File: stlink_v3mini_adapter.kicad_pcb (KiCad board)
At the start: 4 copper layers, 46.5 x 18.5 mm, 19 parts, among them J1 Conn_02x07_Odd_Even, SW1 RST, U3 TLV71333PDBV

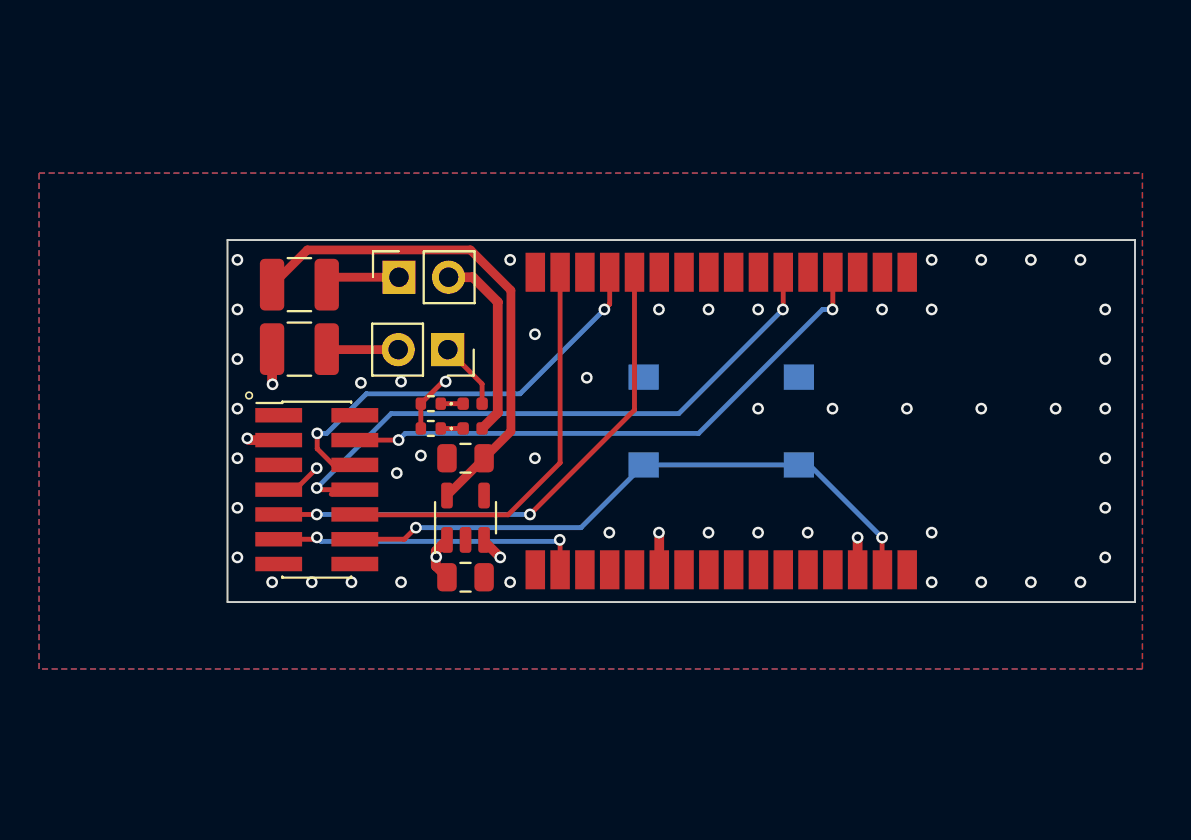
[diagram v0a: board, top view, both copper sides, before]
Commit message: add screws, switch to 2 layers
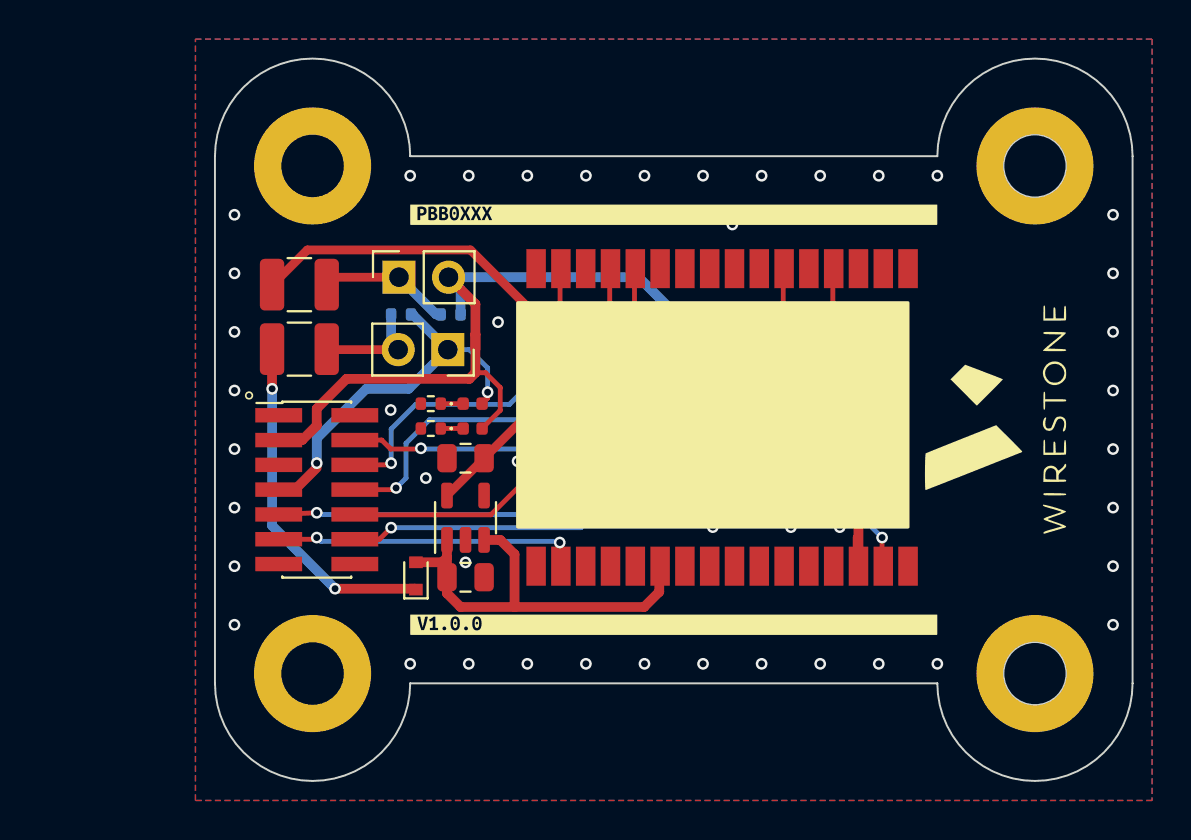
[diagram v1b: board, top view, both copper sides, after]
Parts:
- removed kibuzzard-63CA6A29: G***, kibuzzard-63CA6A29
- removed kibuzzard-63CA6A34: G***, kibuzzard-63CA6A34
- added D3: D_Schottky, Diode_SMD:D_SOD-523, F.Cu at (66.3, 83.5)
- added G***: LOGO, stlink_v3mini:wirestone, F.Cu at (96.0, 75.5)
- added G***: LOGO, stlink_v3mini:wirestone, B.Cu at (95.5, 75.5)
- added R3: R, Resistor_SMD:R_0402_1005Metric, B.Cu at (68.1, 70.1)
- added R4: R, Resistor_SMD:R_0402_1005Metric, B.Cu at (65.5, 70.1)
- added REF**: MountingHole_3.2mm_M3, MountingHole:MountingHole_3.2mm_M3, F.Cu at (61.0, 62.5)
- added REF**: MountingHole_3.2mm_M3, MountingHole:MountingHole_3.2mm_M3, F.Cu at (98.0, 62.5)
- added REF**: MountingHole_3.2mm_M3, MountingHole:MountingHole_3.2mm_M3, F.Cu at (98.0, 88.5)
- added REF**: MountingHole_3.2mm_M3, MountingHole:MountingHole_3.2mm_M3, F.Cu at (61.0, 88.5)
- added kibuzzard-63CFE4E5: G***, kibuzzard-63CFE4E5, F.Cu at (79.5, 65.0)
- added kibuzzard-63CFE4FD: G***, kibuzzard-63CFE4FD, B.Cu at (101.5, 75.5)
- added kibuzzard-63CFE50C: G***, kibuzzard-63CFE50C, F.Cu at (79.5, 86.0)
- moved U2 0.19 mm to (82.0, 75.4)
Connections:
- C1 pad 1: Net-(U2-5V) -> Net-(D3-A)
- F3 pad 2: Net-(U2-5V) -> Net-(D3-K)
- U2 pad 22: Net-(U2-5V) -> Net-(D3-A)
- U3 pad 1: Net-(U2-5V) -> Net-(D3-A)
- U3 pad 3: Net-(U2-5V) -> Net-(D3-A)
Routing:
- net Net-(U2-5V): track 35.9 -> 0.00 mm, vias 4 -> 0
- net Net-(D3-A): track 0.00 -> 21.6 mm
- net Net-(D3-K): track 0.00 -> 17.8 mm, vias 0 -> 2
- net +3.3V: track 66.8 -> 55.3 mm, vias 2 -> 1
- net /SWCLK: track 22.4 -> 19.1 mm
- net /SWO: track 32.9 -> 29.7 mm
- net GND: track 3.01 -> 0.00 mm, vias 50 -> 52
- net Net-(JP4-A): track 3.86 -> 6.78 mm
- net Net-(JP3-B): track 3.67 -> 5.62 mm
- net Net-(U3-OUT): track 25.7 -> 26.4 mm
- net /TXD: track 21.4 -> 20.9 mm
- net +BATT: track 20.8 -> 20.4 mm, vias 1 -> 2
- removed copper zone on In1.Cu, net GND
- removed copper zone on In2.Cu, net GND
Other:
- board size 46.5 x 18.5 mm -> 47 x 37 mm
- copper layers 4 -> 2

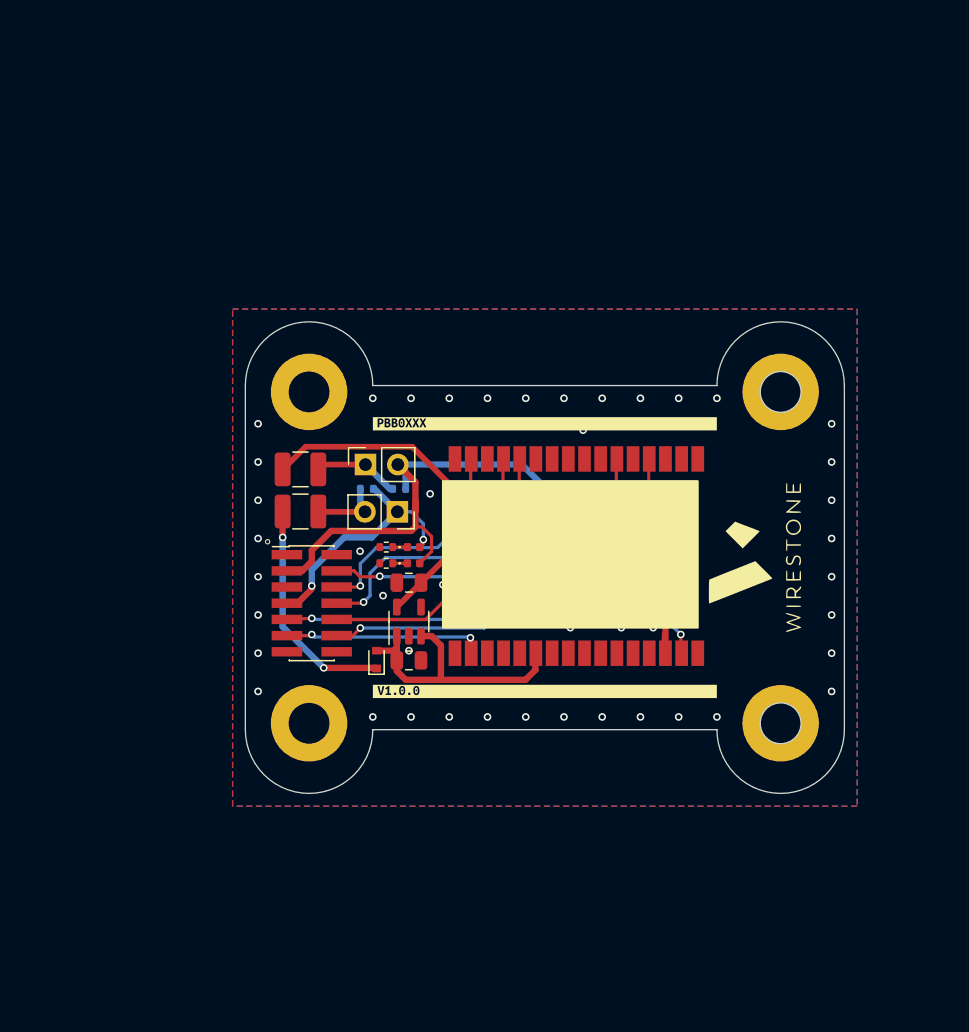
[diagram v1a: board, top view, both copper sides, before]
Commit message: 1.1.0 with tx jumper
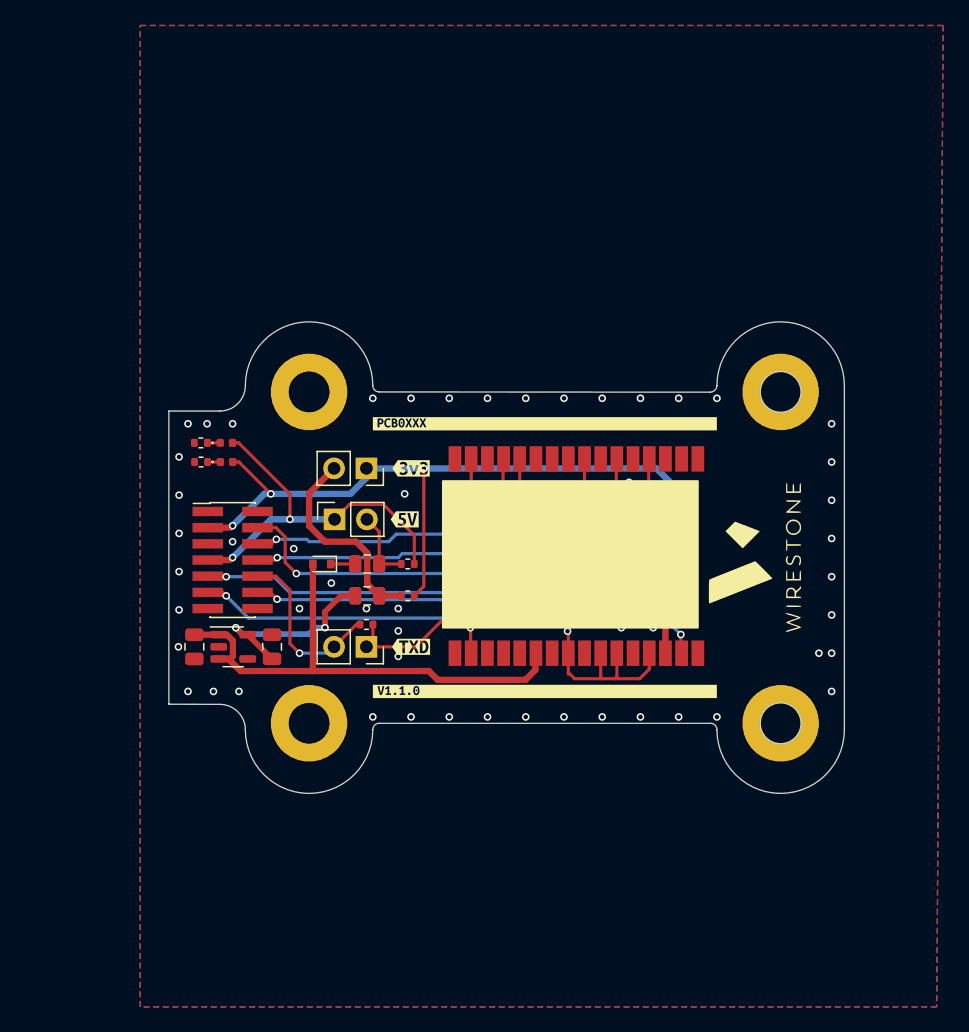
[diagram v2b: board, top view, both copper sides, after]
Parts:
- removed kibuzzard-63CA659A: G***, kibuzzard-63CA659A
- removed kibuzzard-63CA65B1: G***, kibuzzard-63CA65B1
- removed kibuzzard-63CFE4E5: G***, kibuzzard-63CFE4E5
- removed kibuzzard-63CFE4FD: G***, kibuzzard-63CFE4FD
- removed kibuzzard-63CFE50C: G***, kibuzzard-63CFE50C
- added JP1: Jumper_2_Open, Connector_PinSocket_2.54mm:PinSocket_1x02_P2.54mm_Vertical, F.Cu at (65.5, 82.5)
- added R5: 0, Resistor_SMD:R_0402_1005Metric, F.Cu at (65.5, 80.8)
- added kibuzzard-63D24B36: G***, kibuzzard-63D24B36, F.Cu at (79.5, 65.0)
- added kibuzzard-63D24BD9: G***, kibuzzard-63D24BD9, F.Cu at (69.0, 68.5)
- added kibuzzard-649958AB: G***, kibuzzard-649958AB, F.Cu at (69.0, 82.5)
- added kibuzzard-649958B3: G***, kibuzzard-649958B3, F.Cu at (68.5, 72.5)
- added kibuzzard-649958D1: G***, kibuzzard-649958D1, F.Cu at (79.5, 86.0)
- added kibuzzard-6499595A: G***, kibuzzard-6499595A, B.Cu at (101.5, 75.5)
- F2, F3: footprint Fuse:Fuse_1210_3225Metric -> Fuse:Fuse_0805_2012Metric
- R1, R2: value R -> 2k2
- R3, R4: value R -> 0; moved to F.Cu
- moved C1 16.9 mm to (52.0, 82.5), turned to -90 degrees
- moved D2 16.8 mm to (54.5, 66.5)
- moved R2 16.7 mm to (52.5, 66.5)
- moved D1 16.7 mm to (54.5, 68.0)
- moved R1 16.6 mm to (52.5, 68.0)
- moved U3 13.9 mm to (55.0, 82.5), turned to 0 degrees
- moved C2 11.9 mm to (58.1, 82.5), turned to 90 degrees
- moved F2 11.2 mm to (65.6, 78.5)
- moved D3 8.64 mm to (62.0, 76.0), turned to 180 degrees
- moved R3 8.42 mm to (68.7, 78.5)
- moved J1 7.08 mm to (55.0, 75.7)
- moved kibuzzard-63CA65D0 6.97 mm to (87.8, 75.8), turned to -90 degrees
- moved R4 6.71 mm to (68.7, 76.0)
- moved F3 6.66 mm to (65.6, 76.0)
- moved JP3 4.96 mm to (63.0, 72.5), turned to 90 degrees
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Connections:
- F2 pad 2: Net-(JP4-A) -> Net-(JP4-B)
- JP4 pad 1: Net-(JP4-A) -> +3.3V
- JP4 pad 2: +3.3V -> Net-(JP4-B)
- R3 pad 1: Net-(JP4-A) -> Net-(JP4-B)
- U2 pad 12: /RXD -> Net-(JP1-A)
- U2 pad 15: /TXD -> /RXD
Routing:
- net Net-(JP1-A): track 0.00 -> 24.6 mm
- net Net-(D3-A): track 21.6 -> 45.2 mm
- net GND: track 0.00 -> 17.9 mm, vias 52 -> 66
- net Net-(JP4-B): track 0.00 -> 16.3 mm
- net Net-(D3-K): track 17.8 -> 1.92 mm, vias 2 -> 0
- net +3.3V: track 55.3 -> 66.9 mm, vias 1 -> 4
- net Net-(U3-OUT): track 26.4 -> 15.5 mm, vias 0 -> 2
- net +BATT: track 20.4 -> 29.4 mm
- net /SWDIO: track 29.6 -> 38.2 mm
- net /BOOT0: track 16.1 -> 23.8 mm
- net /TXD: track 20.9 -> 13.9 mm, vias 0 -> 1
- net Net-(JP4-A): track 6.78 -> 0.00 mm
- net /SWCLK: track 19.1 -> 25.4 mm
- net /RST: track 32.6 -> 37.1 mm
- net /RXD: track 27.6 -> 31.4 mm
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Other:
- board size 47 x 37 mm -> 53 x 37 mm
- board text removed: "°"

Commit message: wip
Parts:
- added D9: D_Schottky, Diode_SMD:D_SOD-523, F.Cu at (62.5, 78.6)
- added R10: 100, Resistor_SMD:R_0402_1005Metric, F.Cu at (68.5, 81.9)
- added R11: 2k2, Resistor_SMD:R_0402_1005Metric, F.Cu at (54.4, 84.8)
- added R6: 100, Resistor_SMD:R_0402_1005Metric, F.Cu at (68.5, 77.3)
- added R7: 100, Resistor_SMD:R_0402_1005Metric, F.Cu at (68.5, 75.1)
- added R8: 100, Resistor_SMD:R_0402_1005Metric, F.Cu at (68.5, 73.9)
- added R9: 100, Resistor_SMD:R_0402_1005Metric, F.Cu at (68.5, 79.6)
- added kibuzzard-63D24BD9: G***, kibuzzard-63D24BD9, F.Cu at (57.5, 67.9)
- added kibuzzard-66EBEE9F: G***, kibuzzard-66EBEE9F, F.Cu at (58.2, 66.3)
- D1, D2: footprint LED_SMD:LED_0402_1005Metric -> LED_SMD:LED_0603_1608Metric
- R5: value 0 -> O
- moved R5 2.95 mm to (68.5, 80.8)
- moved JP3 2.41 mm to (65.4, 72.6), turned to -90 degrees
- moved D3 1.31 mm to (62.5, 77.2)
- moved kibuzzard-649958AB 0.90 mm to (68.6, 83.3)
- moved kibuzzard-63D24BD9 0.42 mm to (68.7, 68.2)
- moved D2 0.41 mm to (54.9, 66.3)
- moved R4 0.35 mm to (68.5, 76.2)
- moved D1 0.34 mm to (54.9, 67.9)
- moved F3 0.33 mm to (65.6, 76.3)
- moved JP4 0.30 mm to (65.5, 68.2)
- moved kibuzzard-649958B3 0.30 mm to (68.2, 72.5)
- moved R3 0.29 mm to (68.5, 78.5)
- moved R2 0.28 mm to (52.3, 66.3)
- moved R1 0.20 mm to (52.3, 68.0)
- moved F2 0.14 mm to (65.5, 78.4)
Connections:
- C1 pad 1: Net-(D3-A) -> +5V
- C2 pad 1: Net-(U3-OUT) -> Net-(D9-A)
- D3 pad 2: Net-(D3-A) -> +5V
- F2 pad 1: Net-(U3-OUT) -> Net-(D9-K)
- U2 pad 12: Net-(JP1-A) -> Net-(U2-t_vcp_tx)
- U2 pad 13: /SWCLK -> Net-(U2-t_jclk/t_swclk)
- U2 pad 15: /RXD -> Net-(U2-t_vcp_rx)
- U2 pad 19: unconnected-(U2-bridge_gpio1-Pad19) -> /EN_3V3
- U2 pad 22: Net-(D3-A) -> +5V
- U2 pad 4: /SWDIO -> Net-(U2-t_jtms/t_swdio)
- U2 pad 6: /SWO -> Net-(U2-t_jtdo/t_swo)
- U3 pad 1: Net-(D3-A) -> +5V
- U3 pad 3: Net-(D3-A) -> /EN_3V3
- U3 pad 5: Net-(U3-OUT) -> Net-(D9-A)
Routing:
- net Net-(D3-A): track 45.2 -> 0.00 mm
- net +5V: track 0.00 -> 41.2 mm
- net /EN_3V3: track 0.00 -> 26.5 mm, vias 0 -> 2
- net /SWDIO: track 38.2 -> 13.9 mm
- net Net-(U2-t_jtms/t_swdio): track 0.00 -> 23.7 mm, vias 0 -> 2
- net /SWO: track 32.5 -> 11.3 mm
- net Net-(U2-t_jtdo/t_swo): track 0.00 -> 20.4 mm, vias 0 -> 2
- net Net-(JP1-A): track 24.6 -> 4.25 mm
- net Net-(U2-t_vcp_tx): track 0.00 -> 18.7 mm
- net Net-(U3-OUT): track 15.5 -> 0.00 mm, vias 2 -> 0
- net /RXD: track 31.4 -> 16.0 mm
- net Net-(U2-t_vcp_rx): track 0.00 -> 15.3 mm
- net /SWCLK: track 25.4 -> 11.4 mm
- net Net-(U2-t_jclk/t_swclk): track 0.00 -> 13.1 mm, vias 0 -> 2
- net Net-(D9-A): track 0.00 -> 10.4 mm, vias 0 -> 2
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
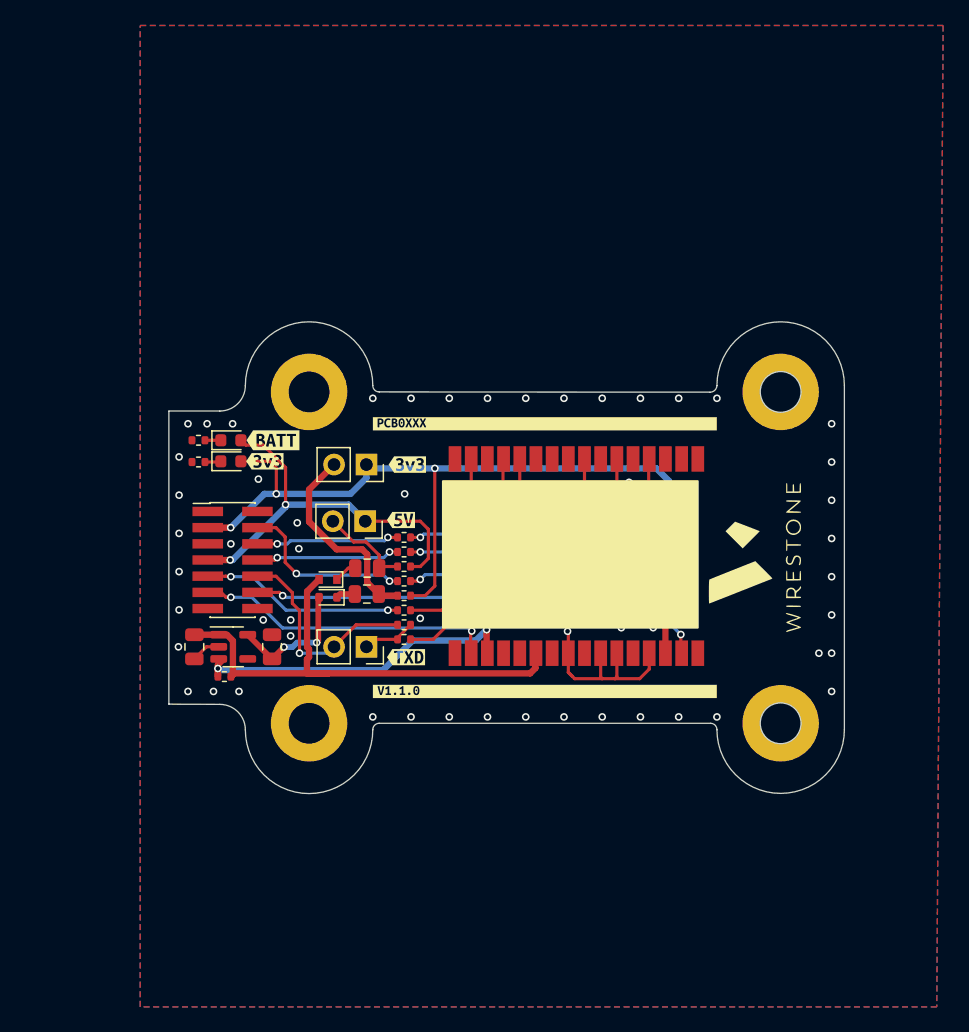
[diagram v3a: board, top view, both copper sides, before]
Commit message: v1.2.0: add simple connector
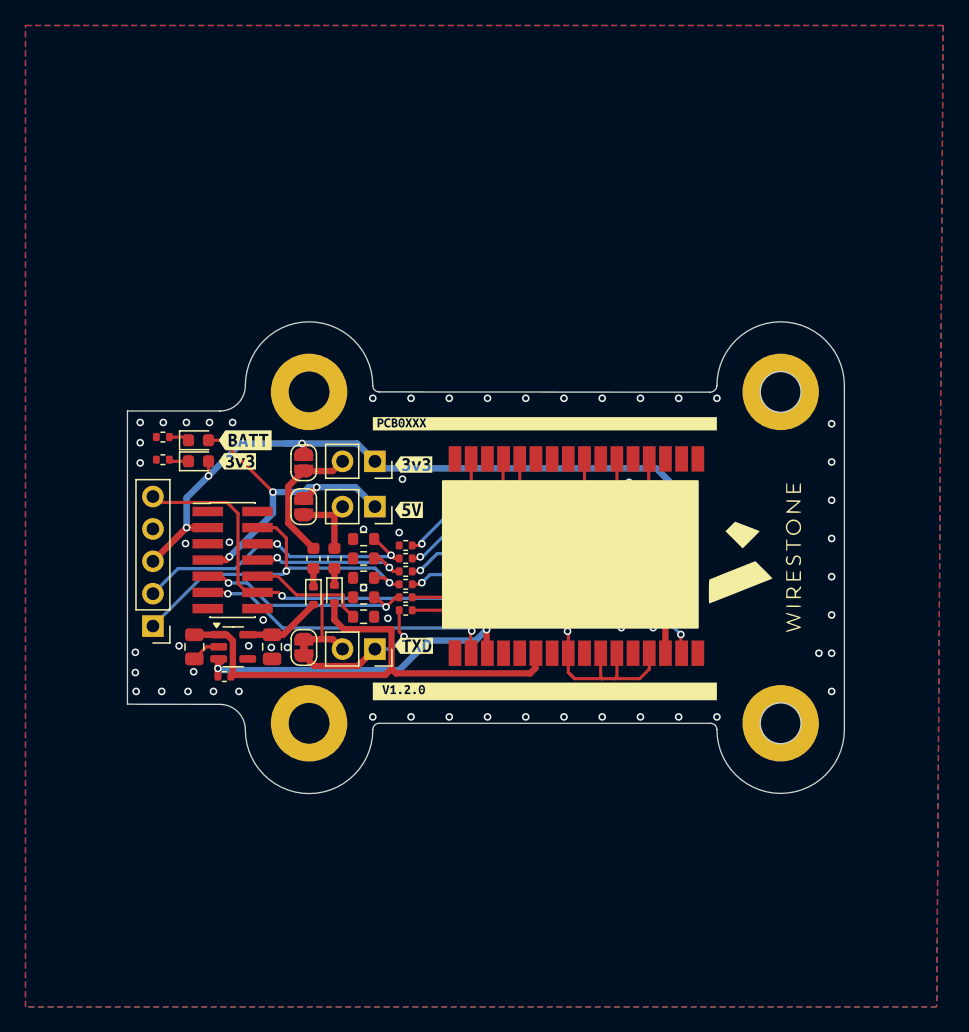
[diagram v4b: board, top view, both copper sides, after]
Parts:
- removed R3, R4: 0, Resistor_SMD:R_0402_1005Metric
- removed R5: O, Resistor_SMD:R_0402_1005Metric
- removed kibuzzard-649958D1: G***, kibuzzard-649958D1
- added D4: PESD3V3L1BA, Resistor_SMD:R_0603_1608Metric, F.Cu at (65.3, 74.0)
- added D5: PESD3V3L1BA, Resistor_SMD:R_0603_1608Metric, F.Cu at (65.3, 75.6)
- added D6: PESD3V3L1BA, Resistor_SMD:R_0603_1608Metric, F.Cu at (65.3, 77.1)
- added D7: PESD3V3L1BA, Resistor_SMD:R_0603_1608Metric, F.Cu at (65.3, 78.6)
- added D8: PESD3V3L1BA, Resistor_SMD:R_0603_1608Metric, F.Cu at (65.3, 80.1)
- added J3: Conn_01x05_Pin, Connector_PinHeader_2.54mm:PinHeader_1x05_P2.54mm_Vertical, F.Cu at (48.8, 80.9)
- added JP2: SolderJumper_2_Bridged, Jumper:SolderJumper-2_P1.3mm_Bridged_RoundedPad1.0x1.5mm, F.Cu at (60.6, 82.5)
- added JP5: SolderJumper_2_Bridged, Jumper:SolderJumper-2_P1.3mm_Open_RoundedPad1.0x1.5mm, F.Cu at (60.6, 71.5)
- added JP7: SolderJumper_2_Bridged, Jumper:SolderJumper-2_P1.3mm_Open_RoundedPad1.0x1.5mm, F.Cu at (60.6, 68.1)
- added R12: 100, Resistor_SMD:R_0402_1005Metric, F.Cu at (68.6, 74.5)
- added kibuzzard-6723780F: G***, kibuzzard-6723780F, F.Cu at (79.5, 86.0)
- added kibuzzard-67239188: G***, kibuzzard-67239188, B.Cu at (52.7, 73.5)
- added kibuzzard-67239190: G***, kibuzzard-67239190, B.Cu at (52.6, 70.9)
- added kibuzzard-67239196: G***, kibuzzard-67239196, B.Cu at (52.7, 76.1)
- added kibuzzard-672391A6: G***, kibuzzard-672391A6, B.Cu at (52.7, 78.5)
- added kibuzzard-672391AE: G***, kibuzzard-672391AE, B.Cu at (52.7, 80.9)
- F2, F3: footprint Fuse:Fuse_0805_2012Metric -> Fuse:Fuse_0603_1608Metric
- moved F2 5.04 mm to (61.3, 75.6), turned to 90 degrees
- moved R2 2.81 mm to (49.5, 66.0)
- moved R1 2.80 mm to (49.5, 67.8)
- moved F3 2.68 mm to (63.0, 75.6), turned to -90 degrees
- moved D1 2.54 mm to (52.3, 67.9)
- moved D2 2.54 mm to (52.3, 66.3)
- moved R10 2.29 mm to (68.6, 79.6)
- moved kibuzzard-66EBEE9F 2.18 mm to (56.0, 66.3)
- moved kibuzzard-63D24BD9 2.16 mm to (55.4, 67.9)
- moved R8 1.66 mm to (68.6, 75.6)
- moved R7 1.53 mm to (68.6, 76.6)
- moved JP3 1.37 mm to (66.2, 71.5)
- moved D3 1.25 mm to (63.0, 78.4), turned to -90 degrees
- moved D9 1.15 mm to (61.3, 78.5), turned to -90 degrees
- moved kibuzzard-649958AB 1.08 mm to (69.2, 82.4)
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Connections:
- SW1 pad 2: GND -> Net-(R12-Pad2)
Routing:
- net Net-(R12-Pad2): track 0.00 -> 18.7 mm, vias 0 -> 3
- net /RST: track 36.9 -> 51.5 mm
- net /SWDIO: track 13.9 -> 28.3 mm
- net /SWCLK: track 11.4 -> 25.1 mm
- net Net-(JP1-A): track 4.25 -> 12.2 mm, vias 0 -> 1
- net +BATT: track 31.2 -> 25.2 mm, vias 2 -> 3
- net Net-(JP4-B): track 15.9 -> 10.7 mm
- net Net-(D9-A): track 10.4 -> 6.13 mm, vias 2 -> 0
- net +3.3V: track 69.5 -> 65.5 mm
- net /SWO: track 11.3 -> 13.1 mm
- net /RXD: track 16.0 -> 17.6 mm
- net /TXD: track 16.9 -> 18.3 mm, vias 1 -> 0
- net Net-(U2-t_vcp_tx): track 18.7 -> 17.7 mm
- net Net-(U2-t_jclk/t_swclk): track 13.1 -> 13.6 mm
- net Net-(U2-t_vcp_rx): track 15.3 -> 14.7 mm
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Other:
- board size 53 x 37 mm -> 56.2 x 37 mm
